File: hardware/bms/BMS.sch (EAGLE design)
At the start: 121 parts, among them Q1 FDY102PZ, Q10 FDY102PZ, Q11 FDY102PZ, Q12 FDY102PZ, Q2 FDY102PZ, Q3 FDY102PZ, Q4 FDY102PZ, Q5 FDY102PZ, Q6 FDY102PZ, Q7 FDY102PZ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

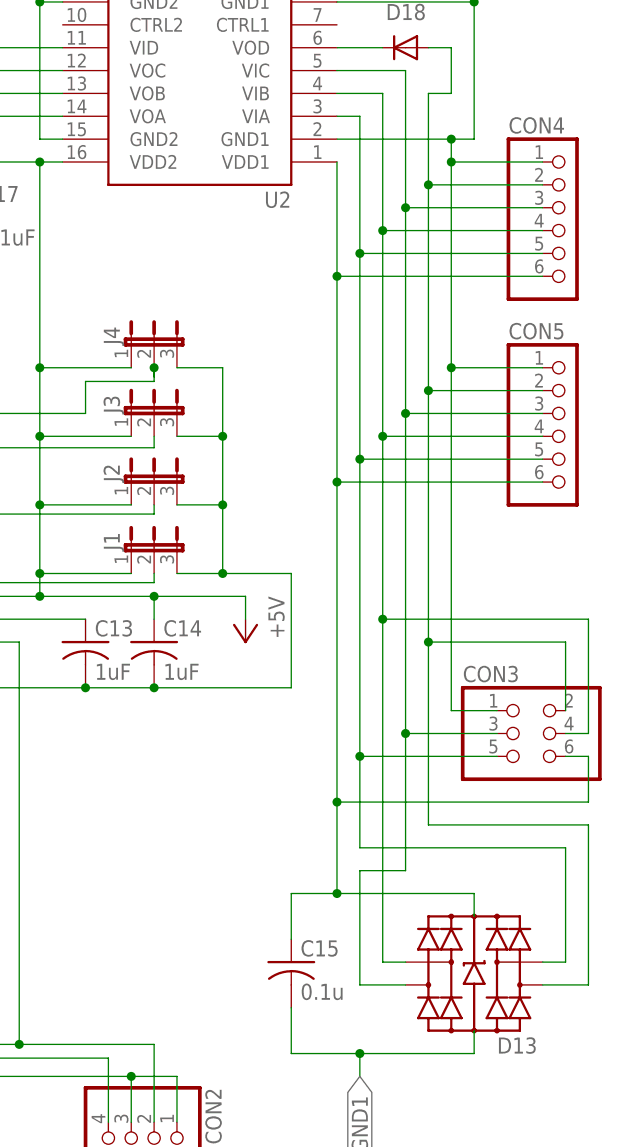
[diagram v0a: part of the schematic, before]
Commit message: Move ESD suppression diode array between inputs and level shift IC. Add decoupling capacitor on level shift IC.
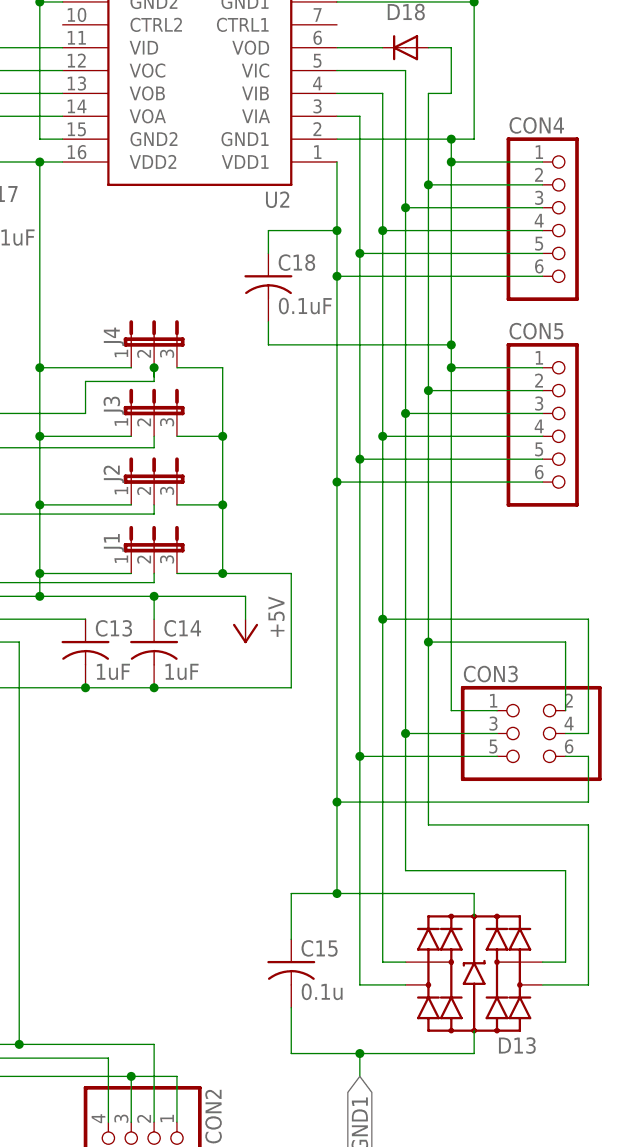
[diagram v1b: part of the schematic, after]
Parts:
- added C18: 0.1uF, rcl:C-USC0603
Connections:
- removed net N$90: C15.1, CON3.6, CON4.6, CON5.6, D13.VCC, U2.VDD1@1
- new net VDD1: C15.1, C18.1, CON3.6, CON4.6, CON5.6, D13.VCC, U2.VDD1@1
- net GND1: now also C18.2
- net N$83: now also D13.IO1; no longer D13.IO3
- net N$86: now also D13.IO3; no longer D13.IO1
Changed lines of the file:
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@@
 <?xml version="1.0" encoding="utf-8"?>
 <!DOCTYPE eagle SYSTEM "eagle.dtd">
-<eagle version="6.3">
+<eagle version="6.4">
 <drawing>
 <settings>
@@
 <part name="GND4" library="supply1" deviceset="GND" device=""/>
 <part name="D13" library="m_diode" deviceset="TPD4E001" device="DBV"/>
+<part name="C18" library="rcl" deviceset="C-US" device="C0603" value="0.1uF"/>
 </parts>
 <sheets>
@@
 <instance part="GND4" gate="1" x="193.04" y="132.08"/>
 <instance part="D13" gate="G$1" x="248.92" y="55.88"/>
+<instance part="C18" gate="G$1" x="226.06" y="134.62"/>
 </instances>
 <busses>
@@
 <wire x1="261.62" y1="96.52" x2="238.76" y2="96.52" width="0.1524" layer="91"/>
 <junction x="238.76" y="96.52"/>
+<wire x1="238.76" y1="58.42" x2="238.76" y2="96.52" width="0.1524" layer="91"/>
 <pinref part="D13" gate="G$1" pin="IO2"/>
-<wire x1="241.3" y1="58.42" x2="238.76" y2="58.42" width="0.1524" layer="91"/>
-<wire x1="238.76" y1="58.42" x2="238.76" y2="96.52" width="0.1524" layer="91"/>
+<wire x1="238.76" y1="58.42" x2="241.3" y2="58.42" width="0.1524" layer="91"/>
 </segment>
 </net>
@@
 <wire x1="241.3" y1="83.82" x2="241.3" y2="68.58" width="0.1524" layer="91"/>
 <junction x="241.3" y="83.82"/>
-<wire x1="241.3" y1="68.58" x2="236.22" y2="68.58" width="0.1524" layer="91"/>
-<wire x1="236.22" y1="68.58" x2="236.22" y2="55.88" width="0.1524" layer="91"/>
-<pinref part="D13" gate="G$1" pin="IO1"/>
-<wire x1="236.22" y1="55.88" x2="241.3" y2="55.88" width="0.1524" layer="91"/>
+<wire x1="241.3" y1="68.58" x2="259.08" y2="68.58" width="0.1524" layer="91"/>
+<wire x1="259.08" y1="68.58" x2="259.08" y2="58.42" width="0.1524" layer="91"/>
+<pinref part="D13" gate="G$1" pin="IO3"/>
+<wire x1="259.08" y1="58.42" x2="256.54" y2="58.42" width="0.1524" layer="91"/>
 </segment>
 </net>
@@
 <pinref part="CON4" gate="A" pin="1"/>
 <wire x1="246.38" y1="147.32" x2="256.54" y2="147.32" width="0.1524" layer="91"/>
-<wire x1="246.38" y1="147.32" x2="246.38" y2="124.46" width="0.1524" layer="91"/>
+<wire x1="246.38" y1="147.32" x2="246.38" y2="127" width="0.1524" layer="91"/>
+<wire x1="246.38" y1="127" x2="246.38" y2="124.46" width="0.1524" layer="91"/>
 <wire x1="246.38" y1="124.46" x2="256.54" y2="124.46" width="0.1524" layer="91"/>
 <junction x="246.38" y="124.46"/>
@@
 <junction x="246.38" y="149.86"/>
 <junction x="246.38" y="147.32"/>
+<pinref part="C18" gate="G$1" pin="2"/>
+<wire x1="226.06" y1="129.54" x2="226.06" y2="127" width="0.1524" layer="91"/>
+<wire x1="226.06" y1="127" x2="246.38" y2="127" width="0.1524" layer="91"/>
+<junction x="246.38" y="127"/>
 </segment>
 <segment>
@@
 </segment>
 </net>
-<net name="N$90" class="0">
+<net name="VDD1" class="0">
 <segment>
 <pinref part="CON5" gate="A" pin="6"/>
@@
 <pinref part="U2" gate="G$1" pin="VDD1@1"/>
 <pinref part="CON4" gate="A" pin="6"/>
-<wire x1="233.68" y1="147.32" x2="233.68" y2="134.62" width="0.1524" layer="91"/>
+<wire x1="233.68" y1="147.32" x2="233.68" y2="139.7" width="0.1524" layer="91"/>
+<wire x1="233.68" y1="139.7" x2="233.68" y2="134.62" width="0.1524" layer="91"/>
 <wire x1="233.68" y1="134.62" x2="233.68" y2="111.76" width="0.1524" layer="91"/>
 <wire x1="233.68" y1="111.76" x2="233.68" y2="76.2" width="0.1524" layer="91"/>
@@
 <wire x1="228.6" y1="66.04" x2="228.6" y2="60.96" width="0.1524" layer="91"/>
 <junction x="233.68" y="66.04"/>
+<pinref part="C18" gate="G$1" pin="1"/>
+<wire x1="226.06" y1="137.16" x2="226.06" y2="139.7" width="0.1524" layer="91"/>
+<wire x1="226.06" y1="139.7" x2="233.68" y2="139.7" width="0.1524" layer="91"/>
+<junction x="233.68" y="139.7"/>
 </segment>
 </net>
@@
 <net name="N$83" class="0">
 <segment>
-<pinref part="D13" gate="G$1" pin="IO3"/>
-<wire x1="259.08" y1="58.42" x2="256.54" y2="58.42" width="0.1524" layer="91"/>
-<wire x1="259.08" y1="58.42" x2="259.08" y2="71.12" width="0.1524" layer="91"/>
-<wire x1="259.08" y1="71.12" x2="236.22" y2="71.12" width="0.1524" layer="91"/>
+<wire x1="236.22" y1="55.88" x2="236.22" y2="81.28" width="0.1524" layer="91"/>
 <pinref part="U2" gate="G$1" pin="VIA"/>
 <wire x1="233.68" y1="152.4" x2="236.22" y2="152.4" width="0.1524" layer="91"/>
@@
 <wire x1="236.22" y1="114.3" x2="236.22" y2="81.28" width="0.1524" layer="91"/>
 <wire x1="236.22" y1="81.28" x2="251.46" y2="81.28" width="0.1524" layer="91"/>
-<wire x1="236.22" y1="71.12" x2="236.22" y2="81.28" width="0.1524" layer="91"/>
 <junction x="236.22" y="81.28"/>
-</segment>
-</net>
+<pinref part="D13" gate="G$1" pin="IO1"/>
+<wire x1="236.22" y1="55.88" x2="241.3" y2="55.88" width="0.1524" layer="91"/>
+</segment>
+</net>
